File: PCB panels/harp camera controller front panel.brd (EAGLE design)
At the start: 133 x 35 mm, 0 parts

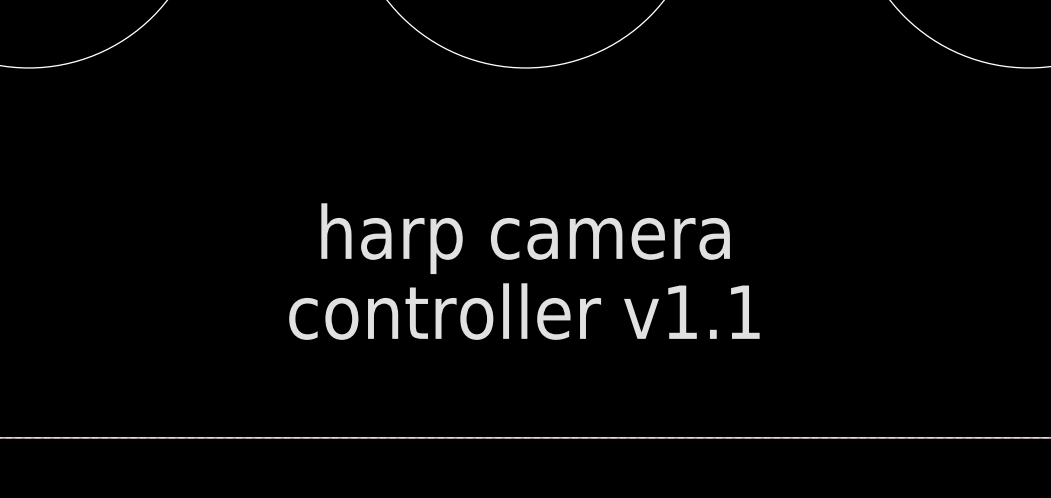
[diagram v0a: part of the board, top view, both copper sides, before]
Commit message: Changed 5V output to 5.3V and released PCB v1.2
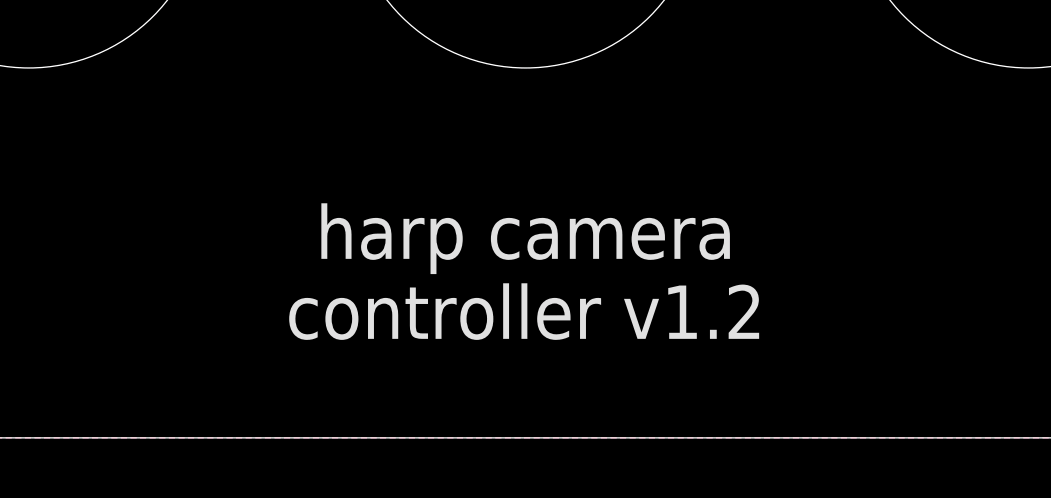
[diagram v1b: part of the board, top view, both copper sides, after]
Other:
- board text added: "harp camera controller v1.2"
- board text removed: "harp camera controller v1.1"
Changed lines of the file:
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@@
 <text x="11.5821125" y="8.50470625" size="1.27" layer="21" font="vector" ratio="15">Powered by:</text>
 <text x="78.450390625" y="3.3" size="1.778" layer="21" font="vector" ratio="18" align="bottom-center">harp camera
-controller v1.1</text>
+controller v1.2</text>
 <wire x1="32.57" y1="12.6" x2="32.27" y2="12.9" width="0" layer="20" curve="-90"/>
 <wire x1="32.27" y1="12.9" x2="32.27" y2="26.2" width="0" layer="20"/>
